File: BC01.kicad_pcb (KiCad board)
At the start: 2 copper layers, 60.3 x 55.9 mm, 2 parts, among them J1 Conn_02x20_Odd_Even, J2 Conn_02x13_Odd_Even

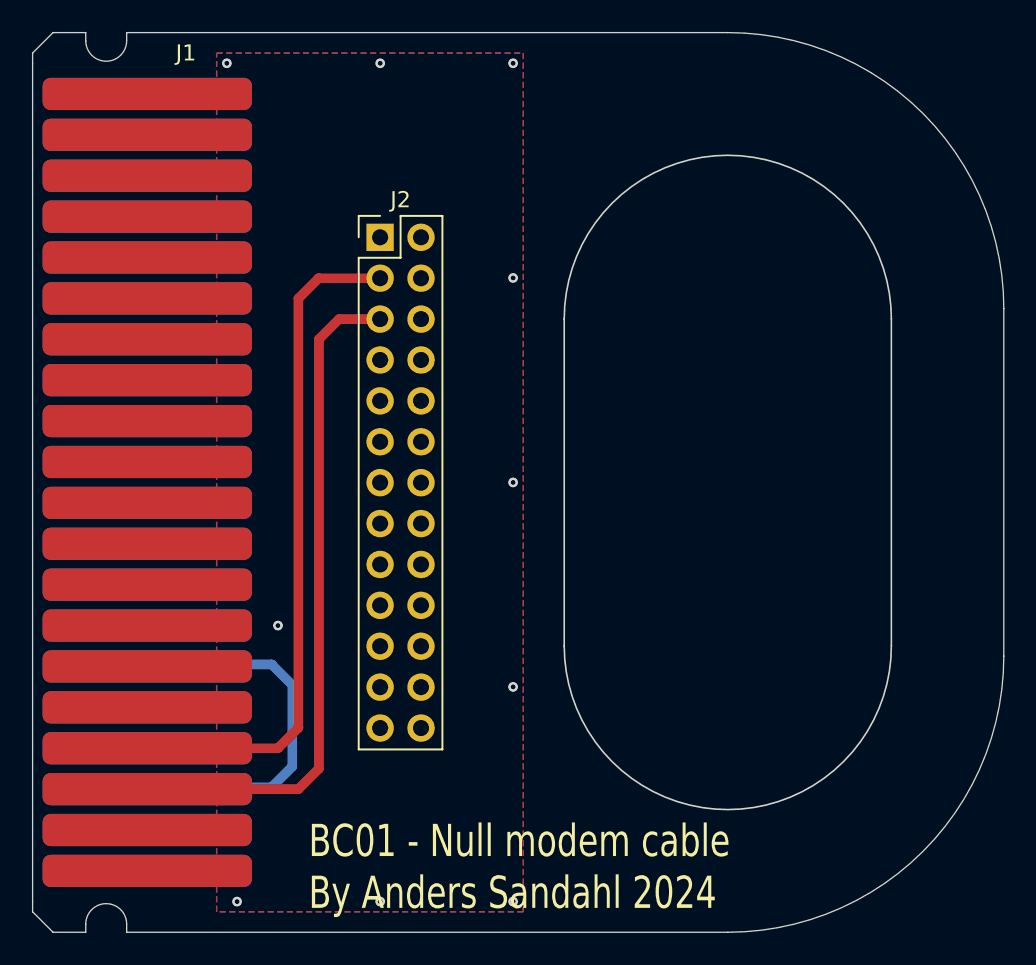
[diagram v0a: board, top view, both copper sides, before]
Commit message: Made it really fit in a PDP-8E
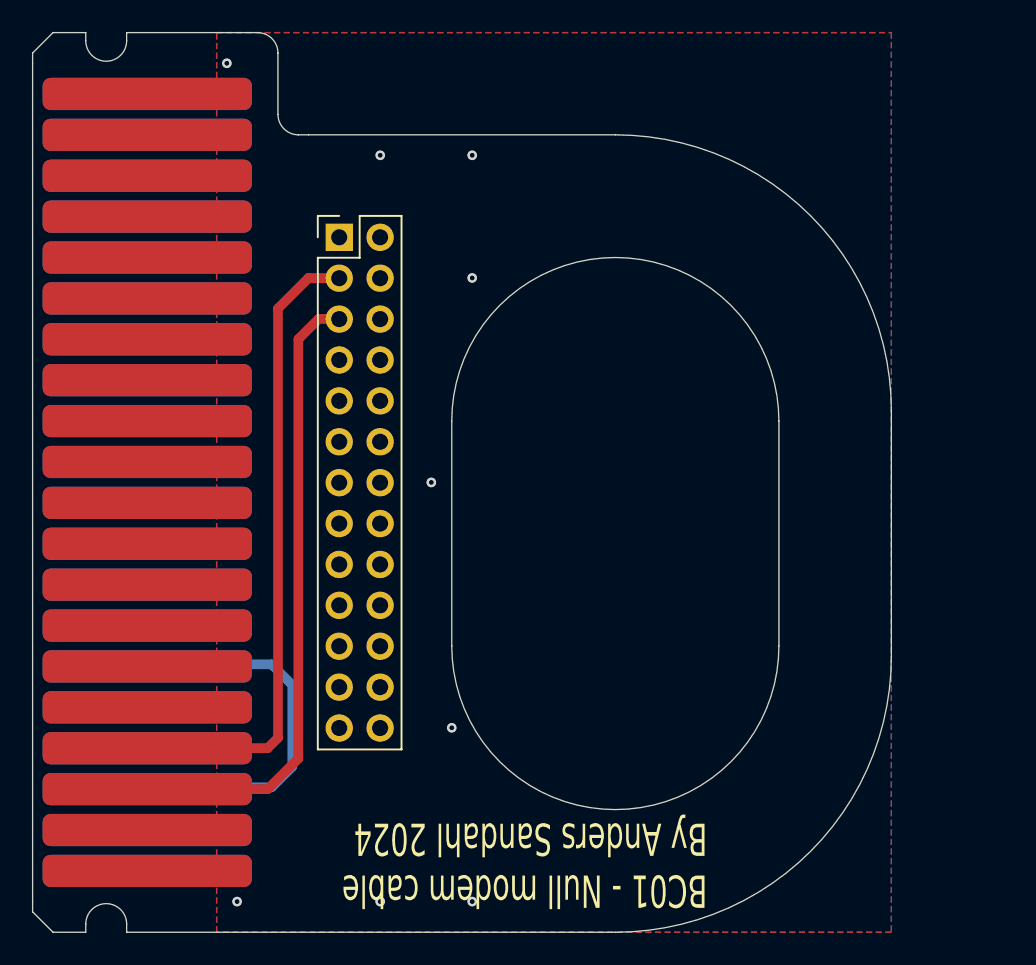
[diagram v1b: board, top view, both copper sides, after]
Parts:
- moved J2 2.54 mm to (139.7, 73.7)
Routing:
- net TxD: track 42.2 -> 39.3 mm
- net RxD: track 42.2 -> 39.7 mm
- net GND: vias 10 -> 9
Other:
- board size 60.3 x 55.9 mm -> 53.3 x 55.9 mm
